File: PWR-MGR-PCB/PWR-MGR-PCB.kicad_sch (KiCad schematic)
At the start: 0 parts

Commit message: begin v2, update schematic
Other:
- sheet PWR-MGR-01 ports: added 5V; removed none
- sheet Physical_Interface ports: added 5V; removed none
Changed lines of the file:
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@@
 (kicad_sch
-	(version 20250114)
+	(version 20260306)
 	(generator "eeschema")
-	(generator_version "9.0")
+	(generator_version "10.0")
 	(paper "A4")
 	(title_block
@@
 	(wire
 		(pts
+			(xy 148.59 106.68) (xy 163.83 106.68)
+		)
+		(stroke
+			(width 0)
+			(type default)
+		)
+	)
+	(wire
+		(pts
 			(xy 148.59 100.33) (xy 163.83 100.33)
 		)
@@
 	(sheet
 		(at 125.73 86.36)
-		(size 22.86 17.78)
+		(size 22.86 26.67)
 		(exclude_from_sim no)
 		(in_bom yes)
@@
 		)
 		(fill
-			(color 0 0 0 0.0000)
+			(color 0 0 0 0)
 		)
 		(property "Sheetname" "Physical_Interface"
 			(at 125.73 85.6484 0)
+			(show_name no)
+			(do_not_autoplace no)
 			(effects
 				(font
@@
 		)
 		(property "Sheetfile" "output.kicad_sch"
-			(at 125.73 104.7246 0)
+			(at 125.73 113.6146 0)
+			(show_name no)
+			(do_not_autoplace no)
 			(effects
 				(font
@@
 		(pin "BAT+" input
 			(at 148.59 97.79 0)
+			(effects
+				(font
+					(size 1.27 1.27)
+				)
+				(justify right)
+			)
+		)
+		(pin "5V" input
+			(at 148.59 106.68 0)
 			(effects
 				(font
@@
 	(sheet
 		(at 163.83 85.09)
-		(size 21.59 19.05)
+		(size 21.59 27.94)
 		(exclude_from_sim no)
 		(in_bom yes)
@@
 		)
 		(fill
-			(color 0 0 0 0.0000)
+			(color 0 0 0 0)
 		)
 		(property "Sheetname" "PWR-MGR-01"
 			(at 163.83 84.3784 0)
+			(show_name no)
+			(do_not_autoplace no)
 			(effects
 				(font
@@
 		)
 		(property "Sheetfile" "pwr-mgr-01.kicad_sch"
-			(at 163.83 104.7246 0)
+			(at 163.83 113.6146 0)
+			(show_name no)
+			(do_not_autoplace no)
 			(effects
 				(font
@@
 			(effects
 				(font
+					(size 1.27 1.27)
+				)
+				(justify left)
+			)
+		)
+		(pin "5V" output
+			(at 163.83 106.68 180)
+			(effects
+				(font

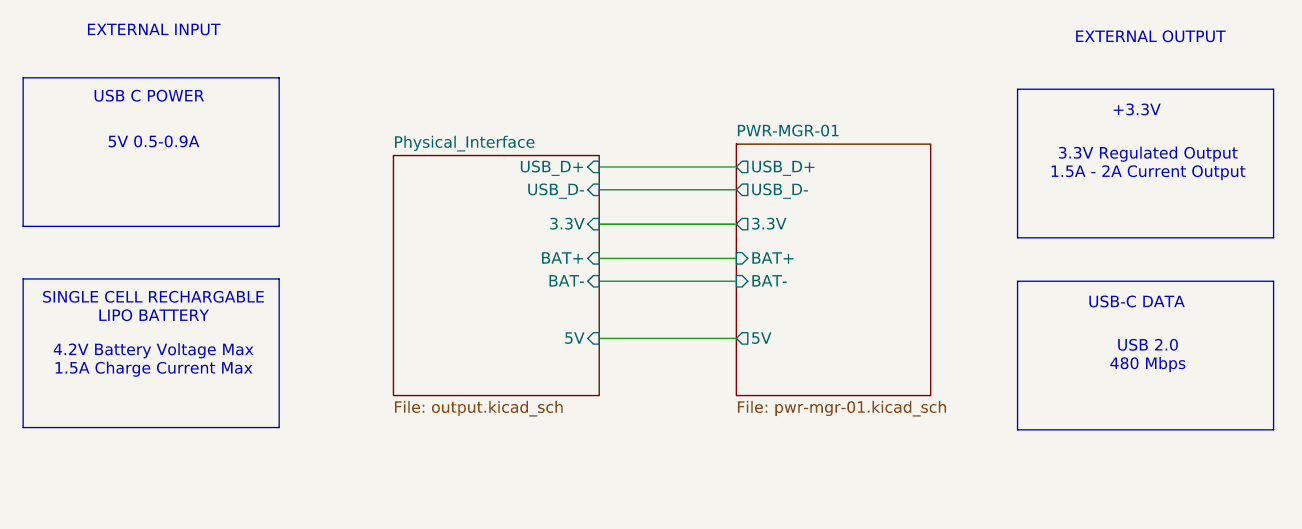
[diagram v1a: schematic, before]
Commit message: complete schematic
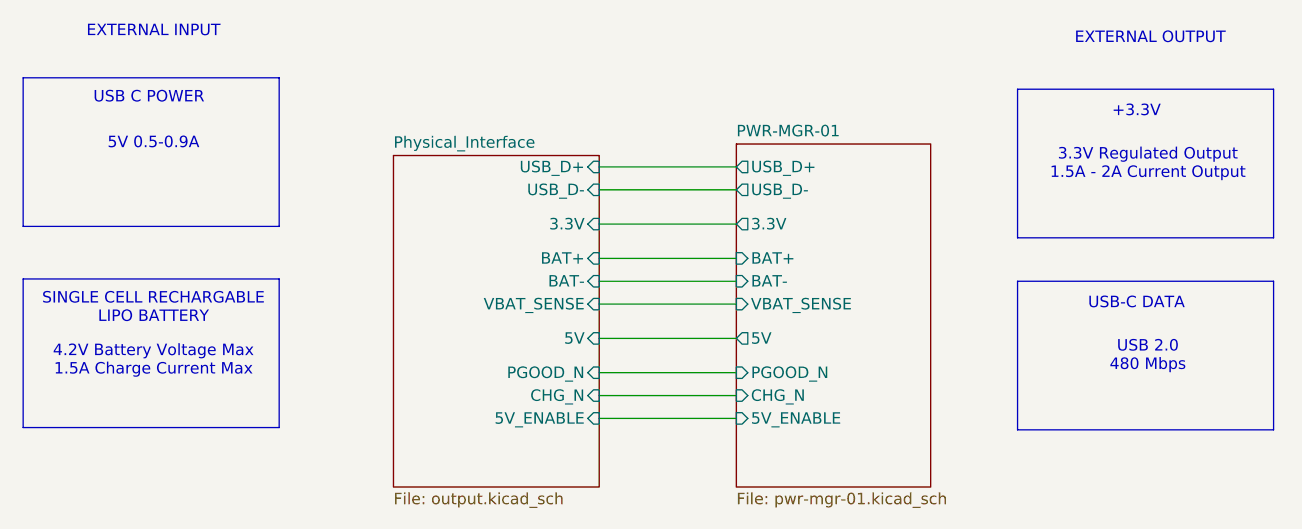
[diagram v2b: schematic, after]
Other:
- sheet PWR-MGR-01 ports: added 5V_ENABLE, CHG_N, PGOOD_N, VBAT_SENSE; removed none
- sheet Physical_Interface ports: added 5V_ENABLE, CHG_N, PGOOD_N, VBAT_SENSE; removed none
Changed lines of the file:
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@@
+	(wire
+		(pts
+			(xy 148.59 102.87) (xy 163.83 102.87)
+		)
+		(stroke
+			(width 0)
+			(type default)
+		)
+	)
+	(wire
+		(pts
+			(xy 148.59 110.49) (xy 163.83 110.49)
+		)
+		(stroke
+			(width 0)
+			(type default)
+		)
+	)
+	(wire
+		(pts
+			(xy 148.59 115.57) (xy 163.83 115.57)
+		)
+		(stroke
+			(width 0)
+			(type default)
+		)
+	)
 	(wire
 		(pts
 			(xy 148.59 90.17) (xy 163.83 90.17)
+		)
+		(stroke
+			(width 0)
+			(type default)
+		)
+	)
+	(wire
+		(pts
+			(xy 148.59 113.03) (xy 163.83 113.03)
 		)
 		(stroke
@@
 	(sheet
 		(at 125.73 86.36)
-		(size 22.86 26.67)
+		(size 22.86 36.83)
 		(exclude_from_sim no)
 		(in_bom yes)
@@
 		)
 		(property "Sheetfile" "output.kicad_sch"
-			(at 125.73 113.6146 0)
+			(at 125.73 123.7746 0)
 			(show_name no)
 			(do_not_autoplace no)
@@
 		(pin "5V" input
 			(at 148.59 106.68 0)
+			(effects
+				(font
+					(size 1.27 1.27)
+				)
+				(justify right)
+			)
+		)
+		(pin "PGOOD_N" input
+			(at 148.59 110.49 0)
+			(effects
+				(font
+					(size 1.27 1.27)
+				)
+				(justify right)
+			)
+		)
+		(pin "CHG_N" input
+			(at 148.59 113.03 0)
+			(effects
+				(font
+					(size 1.27 1.27)
+				)
+				(justify right)
+			)
+		)
+		(pin "5V_ENABLE" input
+			(at 148.59 115.57 0)
+			(effects
+				(font
+					(size 1.27 1.27)
+				)
+				(justify right)
+			)
+		)
+		(pin "VBAT_SENSE" input
+			(at 148.59 102.87 0)
 			(effects
 				(font
@@
 	(sheet
 		(at 163.83 85.09)
-		(size 21.59 27.94)
+		(size 21.59 38.1)
 		(exclude_from_sim no)
 		(in_bom yes)
@@
 		)
 		(property "Sheetfile" "pwr-mgr-01.kicad_sch"
-			(at 163.83 113.6146 0)
+			(at 163.83 123.7746 0)
 			(show_name no)
 			(do_not_autoplace no)
@@
 			(effects
 				(font
+					(size 1.27 1.27)
+				)
+				(justify left)
+			)
+		)
+		(pin "CHG_N" input
+			(at 163.83 113.03 180)
+			(effects
+				(font
+					(size 1.27 1.27)
+				)
+				(justify left)
+			)
+		)
+		(pin "PGOOD_N" input
+			(at 163.83 110.49 180)
+			(effects
+				(font
+					(size 1.27 1.27)
+				)
+				(justify left)
+			)
+		)
+		(pin "5V_ENABLE" input
+			(at 163.83 115.57 180)
+			(effects
+				(font
+					(size 1.27 1.27)
+				)
+				(justify left)
+			)
+		)
+		(pin "VBAT_SENSE" input
+			(at 163.83 102.87 180)
+			(effects
+				(font
